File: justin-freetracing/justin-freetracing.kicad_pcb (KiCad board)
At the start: 2 copper layers, 237.6 x 136.2 mm, 129 parts, among them J1 DB15_Female_HighDensity, J2 Conn_02x03_Odd_Even, J3 Conn_01x08_MountingPin, J5 Barrel_Jack_Switch_Pin3Ring, K1 SW_Push, K10 SW_Push, K11 SW_Push, K12 SW_Push, K13 SW_Push, K14 SW_Push, K15 SW_Push, K16 SW_Push, K17 SW_Push, K18 SW_Push, K19 SW_Push, K2 SW_Push, K20 SW_Push, K21 SW_Push, K22 SW_Push, K23 SW_Push, K24 SW_Push, K25 SW_Push, K26 SW_Push, K27 SW_Push, K28 SW_Push, K29 SW_Push, K3 SW_Push, K30 SW_Push, K31 SW_Push, K32 SW_Push, K33 SW_Push, K34 SW_Push, K35 SW_Push, K36 SW_Push, K37 SW_Push, K38 SW_Push, K39 SW_Push, K4 SW_Push, K40 SW_Push, K41 SW_Push, K42 SW_Push, K43 SW_Push, K44 SW_Push, K45 SW_Push, K46 SW_Push, K47 SW_Push, K48 SW_Push, K49 SW_Push, K5 SW_Push, K6 SW_Push, K7 SW_Push, K8 SW_Push, K9 SW_Push, U1 ATmega1284-P, Y1 20MHz

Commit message: Additional
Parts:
- added U2: ICE40UL1K-SWG16, Package_CSP:WLCSP-16_1.409x1.409mm_P0.35mm, F.Cu at (46.8, 91.4)
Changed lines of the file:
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@@
   (net 95 "Net-(D50-Pad1)")
   (net 96 "Net-(C3-Pad1)")
+  (net 97 "unconnected-(U2-PadA1)")
+  (net 98 "unconnected-(U2-PadA2)")
+  (net 99 "unconnected-(U2-PadA3)")
+  (net 100 "unconnected-(U2-PadA4)")
+  (net 101 "unconnected-(U2-PadB1)")
+  (net 102 "unconnected-(U2-PadB2)")
+  (net 103 "unconnected-(U2-PadB3)")
+  (net 104 "unconnected-(U2-PadB4)")
+  (net 105 "unconnected-(U2-PadC1)")
+  (net 106 "unconnected-(U2-PadC2)")
+  (net 107 "unconnected-(U2-PadC3)")
+  (net 108 "unconnected-(U2-PadC4)")
+  (net 109 "unconnected-(U2-PadD1)")
+  (net 110 "unconnected-(U2-PadD2)")
+  (net 111 "unconnected-(U2-PadD3)")
+  (net 112 "unconnected-(U2-PadD4)")
   (footprint "Button_Switch_Keyboard:SW_Cherry_MX_1.00u_PCB" (layer "F.Cu")
     (at 139.7 139.7)
@@
     (pad "" np_thru_hole circle locked (at 0 0) (size 2.1 2.1) (drill 2.1) (layers *.Cu *.Mask))
   )
+  (footprint "Package_CSP:WLCSP-16_1.409x1.409mm_P0.35mm" (layer "F.Cu")
+    (at 46.75 91.39)
+    (descr "WLCSP-16, 1.409x1.409mm, 16 Ball, 4x4 Layout, 0.35mm Pitch, http://www.latticesemi.com/view_document?document_id=213")
+    (tags "CSP 16 0.35")
+    (property "Sheetfile" "justin-freetracing.kicad_sch")
+    (property "Sheetname" "")
+    (attr smd)
+    (fp_text reference "U2" (at 0 -1.7045) (layer "F.SilkS")
+      (effects (font (size 1 1) (thickness 0.15)))
+    )
+    (fp_text value "ICE40UL1K-SWG16" (at 0 1.7045) (layer "F.Fab")
+      (effects (font (size 1 1) (thickness 0.15)))
+    )
+    (fp_text user "${REFERENCE}" (at 0 0) (layer "F.Fab")
+      (effects (font (size 0.33 0.33) (thickness 0.0495)))
+    )
+    (fp_line (start 0.8145 -0.8145) (end 0.8145 0.8145) (layer "F.SilkS") (width 0.12))
+    (fp_line (start -0.46225 -0.8145) (end 0.8145 -0.8145) (layer "F.SilkS") (width 0.12))
+    (fp_line (start -0.8145 0.8145) (end -0.8145 -0.46225) (layer "F.SilkS") (width 0.12))
+    (fp_line (start 0.8145 0.8145) (end -0.8145 0.8145) (layer "F.SilkS") (width 0.12))
+    (fp_line (start -1.71 1.71) (end 1.71 1.71) (layer "F.CrtYd") (width 0.05))
+    (fp_line (start 1.71 -1.71) (end -1.71 -1.71) (layer "F.CrtYd") (width 0.05))
+    (fp_line (start 1.71 1.71) (end 1.71 -1.71) (layer "F.CrtYd") (width 0.05))
+    (fp_line (start -1.71 -1.71) (end -1.71 1.71) (layer "F.CrtYd") (width 0.05))
+    (fp_line (start -0.7045 0.7045) (end -0.7045 -0.35225) (layer "F.Fab") (width 0.1))
+    (fp_line (start -0.35225 -0.7045) (end 0.7045 -0.7045) (layer "F.Fab") (width 0.1))
+    (fp_line (start 0.7045 0.7045) (end -0.7045 0.7045) (layer "F.Fab") (width 0.1))
+    (fp_line (start 0.7045 -0.7045) (end 0.7045 0.7045) (layer "F.Fab") (width 0.1))
+    (fp_line (start -0.7045 -0.35225) (end -0.35225 -0.7045) (layer "F.Fab") (width 0.1))
+    (pad "A1" smd circle locked (at -0.525 -0.525) (size 0.2 0.2) (layers "F.Cu" "F.Paste" "F.Mask")
+      (net 97 "unconnected-(U2-PadA1)") (pinfunction "IRLED") (pintype "bidirectional"))
+    (pad "A2" smd circle locked (at -0.175 -0.525) (size 0.2 0.2) (layers "F.Cu" "F.Paste" "F.Mask")
+      (net 98 "unconnected-(U2-PadA2)") (pinfunction "BARCODE") (pintype "bidirectional"))
+    (pad "A3" smd circle locked (at 0.175 -0.525) (size 0.2 0.2) (layers "F.Cu" "F.Paste" "F.Mask")
+      (net 99 "unconnected-(U2-PadA3)") (pinfunction "GND") (pintype "power_in"))
+    (pad "A4" smd circle locked (at 0.525 -0.525) (size 0.2 0.2) (layers "F.Cu" "F.Paste" "F.Mask")
+      (net 100 "unconnected-(U2-PadA4)") (pinfunction "RGB1") (pintype "bidirectional"))
+    (pad "B1" smd circle locked (at -0.525 -0.175) (size 0.2 0.2) (layers "F.Cu" "F.Paste" "F.Mask")
+      (net 101 "unconnected-(U2-PadB1)") (pinfunction "GND_LED") (pintype "power_in"))
+    (pad "B2" smd circle locked (at -0.175 -0.175) (size 0.2 0.2) (layers "F.Cu" "F.Paste" "F.Mask")
+      (net 102 "unconnected-(U2-PadB2)") (pinfunction "CRESET_B") (pintype "input"))
+    (pad "B3" smd circle locked (at 0.175 -0.175) (size 0.2 0.2) (layers "F.Cu" "F.Paste" "F.Mask")
+      (net 103 "unconnected-(U2-PadB3)") (pinfunction "VPP_2V5_VCCIO0") (pintype "power_in"))
+    (pad "B4" smd circle locked (at 0.525 -0.175) (size 0.2 0.2) (layers "F.Cu" "F.Paste" "F.Mask")
+      (net 104 "unconnected-(U2-PadB4)") (pinfunction "RGB0") (pintype "bidirectional"))
+    (pad "C1" smd circle locked (at -0.525 0.175) (size 0.2 0.2) (layers "F.Cu" "F.Paste" "F.Mask")
+      (net 105 "unconnected-(U2-PadC1)") (pinfunction "IOB_16A_SCK") (pintype "bidirectional"))
+    (pad "C2" smd circle locked (at -0.175 0.175) (size 0.2 0.2) (layers "F.Cu" "F.Paste" "F.Mask")
+      (net 106 "unconnected-(U2-PadC2)") (pinfunction "IOB_14A_SO") (pintype "bidirectional"))
+    (pad "C3" smd circle locked (at 0.175 0.175) (size 0.2 0.2) (layers "F.Cu" "F.Paste" "F.Mask")
+      (net 107 "unconnected-(U2-PadC3)") (pinfunction "IOB_8A_G4_CDONE") (pintype "bidirectional"))
+    (pad "C4" smd circle locked (at 0.525 0.175) (size 0.2 0.2) (layers "F.Cu" "F.Paste" "F.Mask")
+      (net 108 "unconnected-(U2-PadC4)") (pinfunction "RGB2") (pintype "bidirectional"))
+    (pad "D1" smd circle locked (at -0.525 0.525) (size 0.2 0.2) (layers "F.Cu" "F.Paste" "F.Mask")
+      (net 109 "unconnected-(U2-PadD1)") (pinfunction "IOB_17B_SS") (pintype "bidirectional"))
+    (pad "D2" smd circle locked (at -0.175 0.525) (size 0.2 0.2) (layers "F.Cu" "F.Paste" "F.Mask")
+      (net 110 "unconnected-(U2-PadD2)") (pinfunction "IOB_15B_SI") (pintype "bidirectional"))
+    (pad "D3" smd circle locked (at 0.175 0.525) (size 0.2 0.2) (layers "F.Cu" "F.Paste" "F.Mask")
+      (net 111 "unconnected-(U2-PadD3)") (pinfunction "VCCIO") (pintype "power_in"))
+    (pad "D4" smd circle locked (at 0.525 0.525) (size 0.2 0.2) (layers "F.Cu" "F.Paste" "F.Mask")
+      (net 112 "unconnected-(U2-PadD4)") (pinfunction "VCC") (pintype "power_in"))
+    (model "${KICAD6_3DMODEL_DIR}/Package_CSP.3dshapes/WLCSP-16_1.409x1.409mm_P0.35mm.wrl"
+      (offset (xyz 0 0 0))
+      (scale (xyz 1 1 1))
+      (rotate (xyz 0 0 0))
+    )
+  )
   (footprint "Button_Switch_Keyboard:SW_Cherry_MX_1.00u_PCB" (layer "F.Cu")
     (at 158.75 101.6)
@@
     (effects (font (size 2 2) (thickness 0.15)))
   )
+  (gr_text "` ~" (at 23.05 129.78) (layer "F.SilkS")
+    (effects (font (size 2 2) (thickness 0.15)))
+  )
   (gr_text "7 &" (at 156.12 110.77) (layer "F.SilkS")
     (effects (font (size 2 2) (thickness 0.15)))
@@
     (effects (font (size 2 2) (thickness 0.15)))
   )
-  (gr_text "` ~" (at 23.05 129.78) (layer "F.SilkS")
-    (effects (font (size 2 2) (thickness 0.15)))
-  )

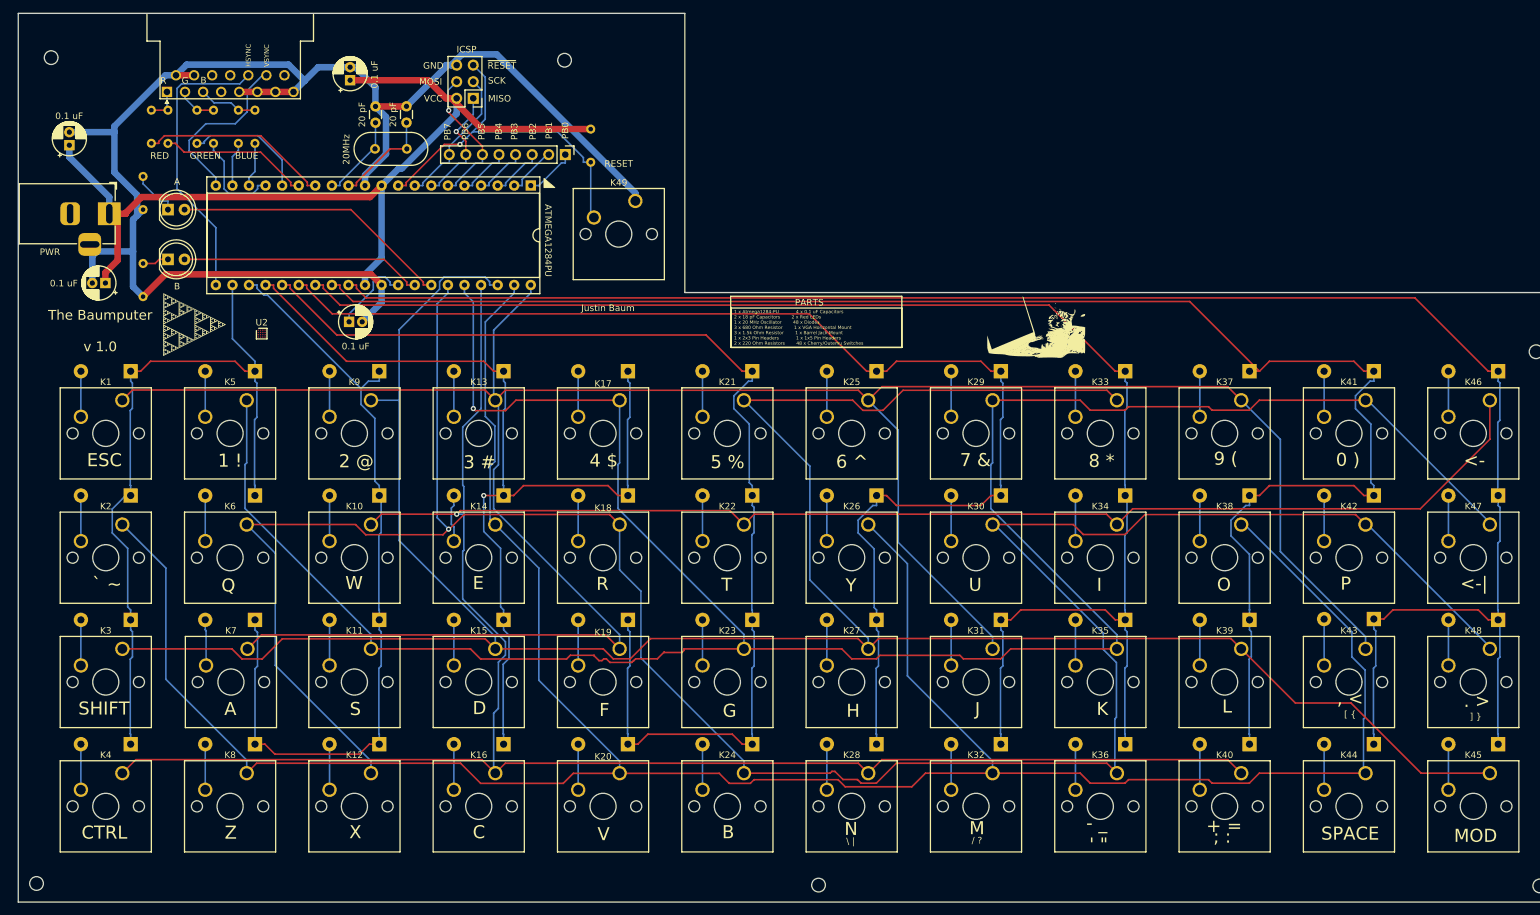
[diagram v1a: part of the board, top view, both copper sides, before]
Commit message: AVR Update
Clang Tidy
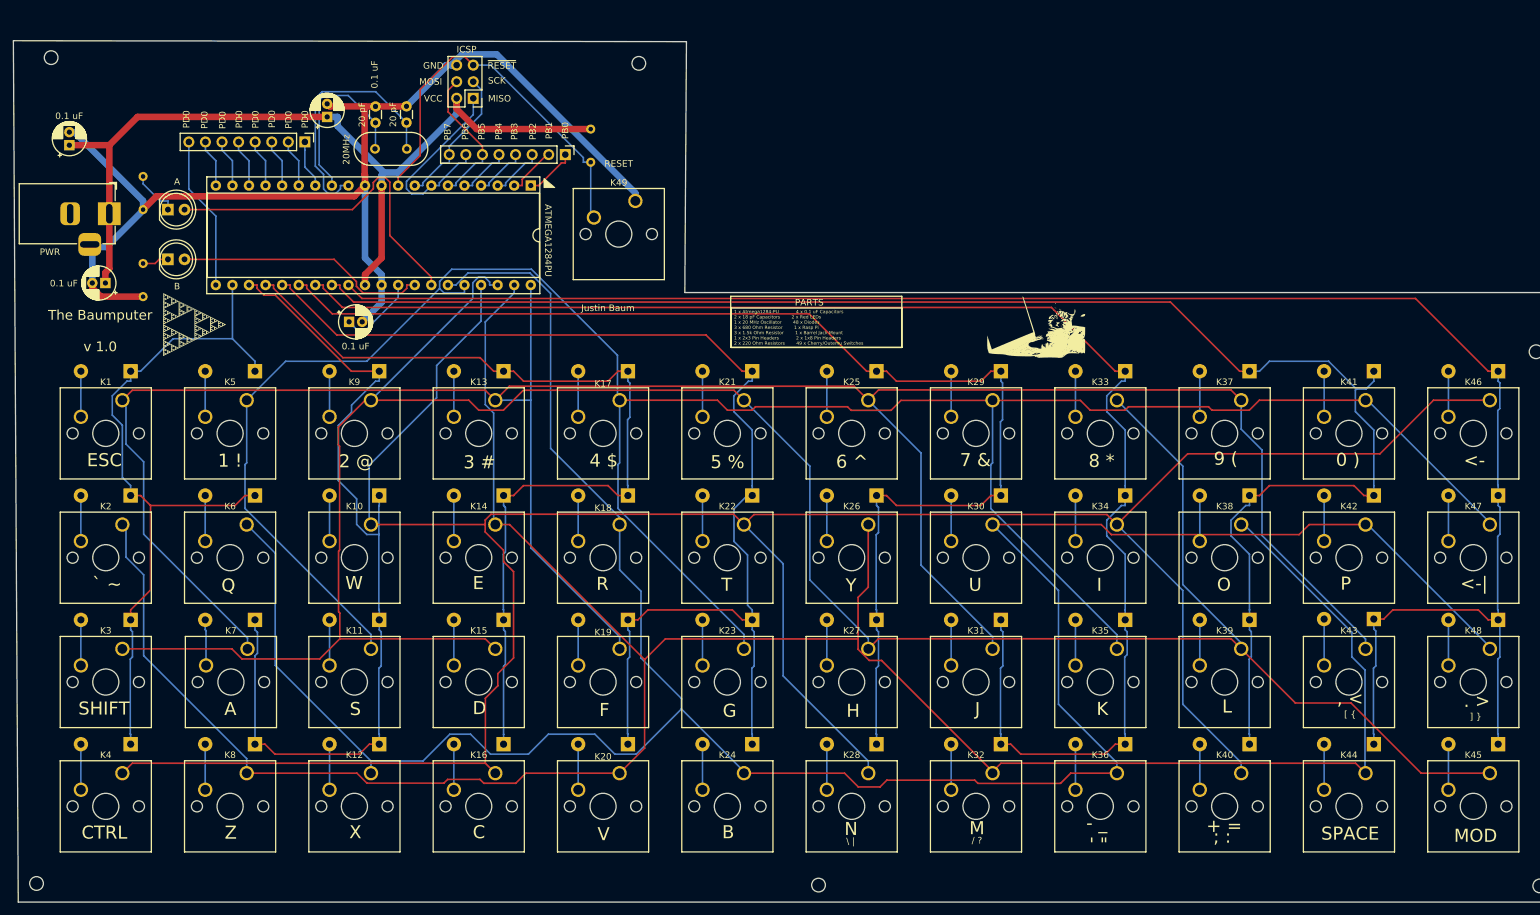
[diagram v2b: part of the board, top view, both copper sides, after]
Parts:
- removed R49, R50, R51: 1.5k, Resistor_THT:R_Axial_DIN0204_L3.6mm_D1.6mm_P5.08mm_Horizontal
- removed R52, R53, R54: 680, Resistor_THT:R_Axial_DIN0204_L3.6mm_D1.6mm_P5.08mm_Horizontal
- removed U2: ICE40UL1K-SWG16, Package_CSP:WLCSP-16_1.409x1.409mm_P0.35mm
- J1: value DB15_Female_HighDensity -> Conn_01x08_MountingPin; footprint Connector_Dsub:DSUB-15_Female_Horizontal_P2.77x2.54mm_EdgePinOffset9.40mm -> Connector_PinHeader_2.54mm:PinHeader_1x08_P2.54mm_Vertical
- moved J1 22.5 mm to (53.4, 62.0), turned to -90 degrees
- moved REF1 11.4 mm to (104.5, 50.0)
- moved C4 6.63 mm to (56.8, 58.2)
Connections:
- J1 pad 1: /RED -> /PD0
- J1 pad 2: /GREEN -> /PD1
- J1 pad 3: /BLUE -> /PD2
- J1 pad 4: unconnected-(J1-Pad4) -> /PD3
- J1 pad 5: GND -> /PD4
- J1 pad 6: GND -> /PD5
- J1 pad 7: GND -> /PD6
- J1 pad 8: GND -> /PD7
- U1 pad 14: Net-(R50-Pad2) -> /PD0
- U1 pad 15: Net-(R54-Pad2) -> /PD1
- U1 pad 16: Net-(R49-Pad2) -> /PD2
- U1 pad 17: Net-(R52-Pad2) -> /PD3
- U1 pad 18: Net-(R51-Pad2) -> /PD4
- U1 pad 19: Net-(R53-Pad2) -> /PD5
- U1 pad 20: /VSYNC -> /PD6
- U1 pad 21: /HSYNC -> /PD7
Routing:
- net GND: track 226.1 -> 174.9 mm
- net /HSYNC: track 44.3 -> 0.00 mm
- net Net-(R50-Pad2): track 29.2 -> 0.00 mm
- net /VSYNC: track 26.5 -> 0.00 mm
- net /KR3: track 442.8 -> 416.8 mm, vias 1 -> 0
- net /KR2: track 408.8 -> 384.6 mm
- net Net-(C2-Pad2): track 15.6 -> 39.7 mm
- net /PD7: track 0.00 -> 23.6 mm
- net Net-(R54-Pad2): track 23.0 -> 0.00 mm
- net /KR1: track 402.1 -> 381.5 mm
- net Net-(R49-Pad2): track 19.2 -> 0.00 mm
- net /KR4: track 385.9 -> 367.0 mm, vias 1 -> 0
- net Net-(C1-Pad2): track 13.3 -> 28.6 mm
- net Net-(R52-Pad2): track 15.2 -> 0.00 mm
- net /KR5: track 383.6 -> 396.3 mm, vias 1 -> 0
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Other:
- board size 237.6 x 136.2 mm -> 238.3 x 132 mm
- board text added: "1 x Atmega1284-PU 4 x 0.1 uF Capacitors 2 x 18 pF Capacitors 2 x Red LEDs 1 x 20 MHz Oscillator 48 x Diodes 3 x 680 Ohm Resistor 1 x Rasp Pi 3 x 1.5k Ohm Resistor 1 x Barrel Jack Mount 1 x 2x3 Pin Headers 2 x 1x8 Pin Headers 2 x 220 Ohm Resistors 49 x Cherry/Outemu Switches"
- board text added: "PD0"
- board text removed: "1 x Atmega1284-PU 4 x 0.1 uF Capacitors 2 x 18 pF Capacitors 2 x Red LEDs 1 x 20 MHz Oscillator 48 x Diodes 3 x 680 Ohm Resistor 1 x VGA Horizontal Mount 3 x 1.5k Ohm Resistor 1 x Barrel Jack Mount 1 x 2x3 Pin Headers 1 x 1x5 Pin Headers 2 x 220 Ohm Resistors 48 x Cherry/Outemu Switches"
- board text removed: "BLUE"
- board text removed: "GREEN"
- board text removed: "HSYNC"
- board text removed: "RED"
- board text removed: "VSYNC"

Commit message: Testing LEDs Live
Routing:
- net /KR1: track 381.5 -> 382.9 mm
- net /KC1: track 135.5 -> 136.5 mm
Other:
- board text added: "PD1"
- board text added: "PD2"
- board text added: "PD3"
- board text added: "PD4"
- board text added: "PD5"
- board text added: "PD6"
- board text added: "PD7"
- board text added: "The Baumputer v 1.1"
- board text removed: "The Baumputer v 1.0"

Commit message: Push
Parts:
- added SW1: SW_SPDT, Connector_PinSocket_2.54mm:PinSocket_1x03_P2.54mm_Vertical, F.Cu at (88.7, 53.1)
- R1, R2, R3: footprint Resistor_THT:R_Axial_DIN0204_L3.6mm_D1.6mm_P5.08mm_Horizontal -> Resistor_THT:R_Axial_DIN0204_L3.6mm_D1.6mm_P7.62mm_Horizontal; moved to F.Cu
- REF1, REF2, REF3, REF4, REF6, REF7: value MountingHole_2.1mm -> MountingHole_2.2mm_M2; footprint MountingHole:MountingHole_2.1mm -> MountingHole:MountingHole_2.2mm_M2
- moved R3 46.5 mm to (143.5, 55.9)
- moved J2 36.1 mm to (43.1, 57.0)
- moved K49 35.7 mm to (139.7, 69.8)
- moved REF1 31.5 mm to (135.9, 53.3)
- moved U1 21.3 mm to (109.2, 69.8)
- moved G3 19.1 mm to (85.1, 77.5)
- moved J3 16.0 mm to (109.2, 64.8)
- moved C1 14.6 mm to (78.7, 57.1)
- moved C2 14.6 mm to (83.5, 57.1)
- moved Y1 14.6 mm to (83.5, 63.7)
- moved J1 14.2 mm to (67.3, 64.8)
- moved C3 13.2 mm to (47.0, 88.9)
- moved C4 12.8 mm to (68.6, 53.3)
- moved D49 4.45 mm to (36.8, 72.4)
- moved D50 4.45 mm to (36.8, 80.0)
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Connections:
- K49 pad 1: GND -> Net-(K49-Pad1)
- K49 pad 2: /~RESET -> GND
- R3 pad 2: /~RESET -> Net-(K49-Pad1)
- U1 pad 9: /~RESET -> Net-(SW1-Pad2)
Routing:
- net VCC: track 134.9 -> 199.6 mm
- net Net-(K49-Pad1): track 0.00 -> 60.8 mm
- net /MOSI: track 22.1 -> 69.9 mm
- net GND: track 174.9 -> 217.2 mm
- net Net-(C3-Pad1): track 12.0 -> 49.0 mm
- net /KR1: track 382.9 -> 419.7 mm
- net /PA7: track 38.9 -> 75.2 mm
- net /PB7: track 22.0 -> 57.7 mm
- net /MISO: track 31.0 -> 60.3 mm
- net /KC3: track 180.6 -> 153.7 mm
- net Net-(C2-Pad2): track 39.7 -> 16.2 mm
- net /KC7: track 280.1 -> 258.8 mm
- net /KC1: track 136.5 -> 115.9 mm
- net /KC2: track 140.8 -> 121.4 mm
- net /KC6: track 248.8 -> 229.4 mm
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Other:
- outline, holes or cut-outs redrawn
- board text added: "220 Ω"
- board text added: "PROGRAM"
- board text added: "RUN"
- board text added: "The Baumputer v 1.2"
- board text removed: "The Baumputer v 1.1"
